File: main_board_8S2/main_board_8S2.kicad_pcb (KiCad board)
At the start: 2 copper layers, 114.3 x 86.4 mm, 47 parts

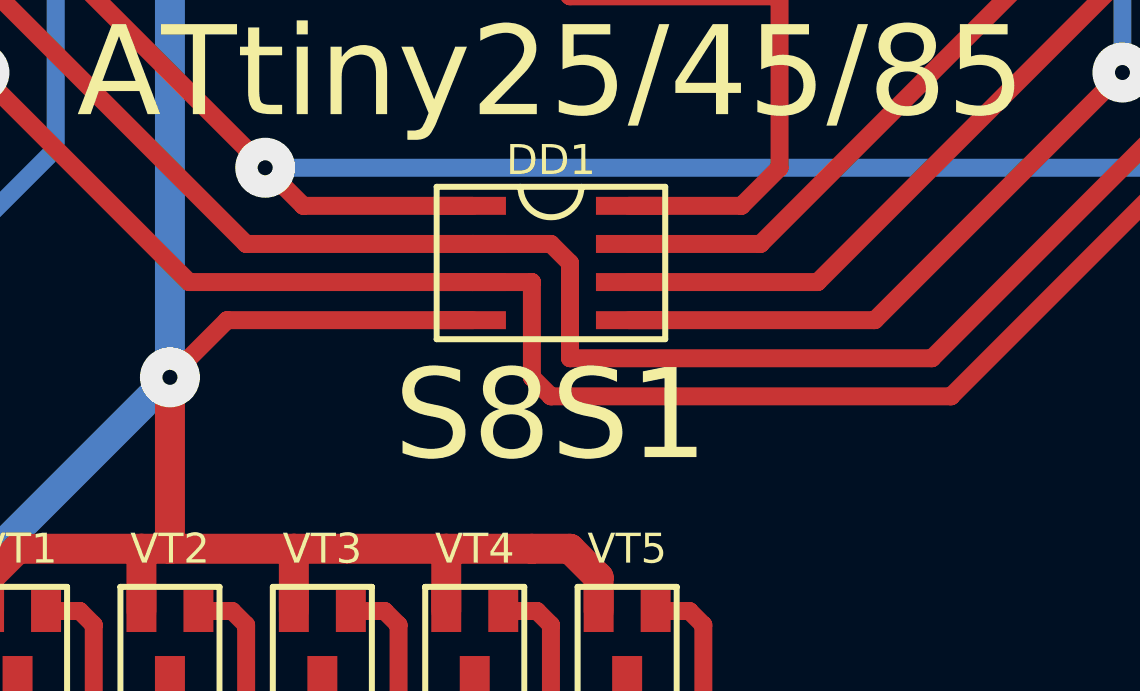
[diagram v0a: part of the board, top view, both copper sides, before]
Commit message: Спроектированы варианты основных плат для МК в корпусах 8P3 и 8S2. Повторно выбраны значения свойсва Placement Type футпринтов
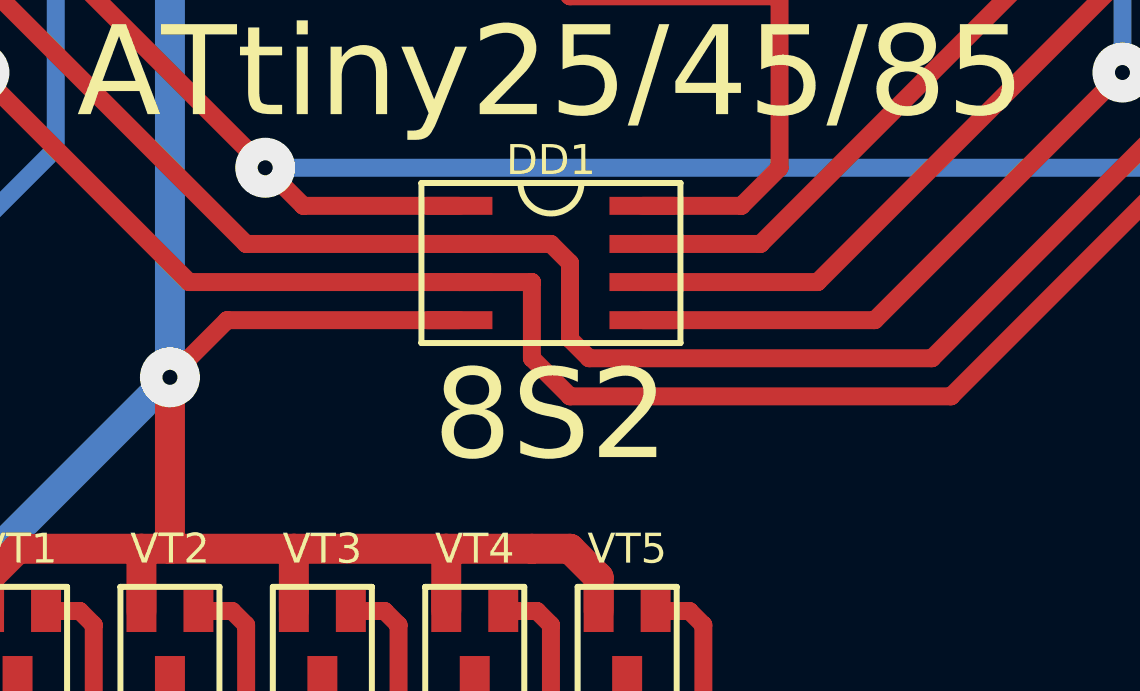
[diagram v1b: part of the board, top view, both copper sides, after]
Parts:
- DD1: value IC_MCU_AVR_TINY_25-45-85_S8S1 -> IC_MCU_AVR_TINY_25-45-85_8S2; footprint KCL:P-SO-08 -> KCL:P-SO-08A
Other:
- board text added: "8S2"
- board text removed: "S8S1"

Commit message: Обновлены УГО ИМС
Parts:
- removed DD1: IC_MCU_AVR_TINY_25-45-85_8S2, KCL:P-SO-08A
- added D1: ATtiny25-20SU, KCL:P-SO-08A, F.Cu at (148.6, 104.1)
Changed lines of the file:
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@@
-(kicad_pcb (version 20171130) (host pcbnew 5.0.0-fee4fd1~66~ubuntu18.04.1)
+(kicad_pcb (version 20171130) (host pcbnew 5.0.2-bee76a0~70~ubuntu18.04.1)
   (general
     (thickness 1.5)
@@
   (title_block
     (title main_board_8S2)
-    (date 2019-02-18)
+    (date 2019-05-15)
     (rev 1)
     (company "Igor Vladimirovich Ivanov")
@@
     (pad_drill 0.762)
     (pad_to_mask_clearance 0.2)
+    (solder_mask_min_width 0.25)
     (aux_axis_origin 0 0)
     (visible_elements 7FFFFFFF)
@@
     (at 148.59 104.14)
     (attr smd)
-    (fp_text reference DD1 (at 0 -3.429) (layer F.SilkS)
-      (effects (font (size 1 1) (thickness 0.2)))
-    )
-    (fp_text value IC_MCU_AVR_TINY_25-45-85_8S2 (at 0 -4.699) (layer F.Fab) hide
+    (fp_text reference D1 (at 0 -3.81) (layer F.SilkS)
+      (effects (font (size 1 1) (thickness 0.2)))
+    )
+    (fp_text value ATtiny25-20SU (at 10.16 0) (layer F.Fab) hide
       (effects (font (size 1 1) (thickness 0.2)))
     )
@@
   (gr_line (start 205.74 60.96) (end 205.74 147.32) (angle 90) (layer Edge.Cuts) (width 0.4))
   (gr_line (start 91.44 60.96) (end 205.74 60.96) (angle 90) (layer Edge.Cuts) (width 0.4))
-  (gr_text ATtiny25/45/85 (at 148.59 97.79) (layer F.SilkS)
+  (gr_text ATtiny25/45/85 (at 148.59 97.155) (layer F.SilkS)
     (effects (font (size 3 3) (thickness 0.6)))
   )
